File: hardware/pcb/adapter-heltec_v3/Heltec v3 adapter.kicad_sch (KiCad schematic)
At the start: 2 parts, among them U1 ESP32_LORA_V2.0

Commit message: Initial boards for raw prototyping
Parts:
- added C1: C_Polarized, Capacitor_THT:CP_Radial_D8.0mm_P3.50mm, symbol Device:C_Polarized
- added C2: C, Capacitor_THT:C_Rect_L4.0mm_W2.5mm_P2.50mm, symbol Device:C
- added J1: Conn_01x02_Pin, Connector_PinHeader_2.54mm:PinHeader_1x02_P2.54mm_Vertical, symbol Connector:Conn_01x02_Pin
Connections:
- net GND: now also U2.1 (GND_A), U2.16 (GND_D), U2.6 (GND_B), C1.2, C2.2, J1.2 (Pin_2)
- net VDD: now also U2.2 (VBAT_A), C1.1, C2.1, J1.1 (Pin_1); no longer U1.J2_3 (VEXT), U1.J2_4 (VEXT), U2.12 (VBAT_C)
- new net VEXT: U1.J2_3 (VEXT), U1.J2_4 (VEXT)

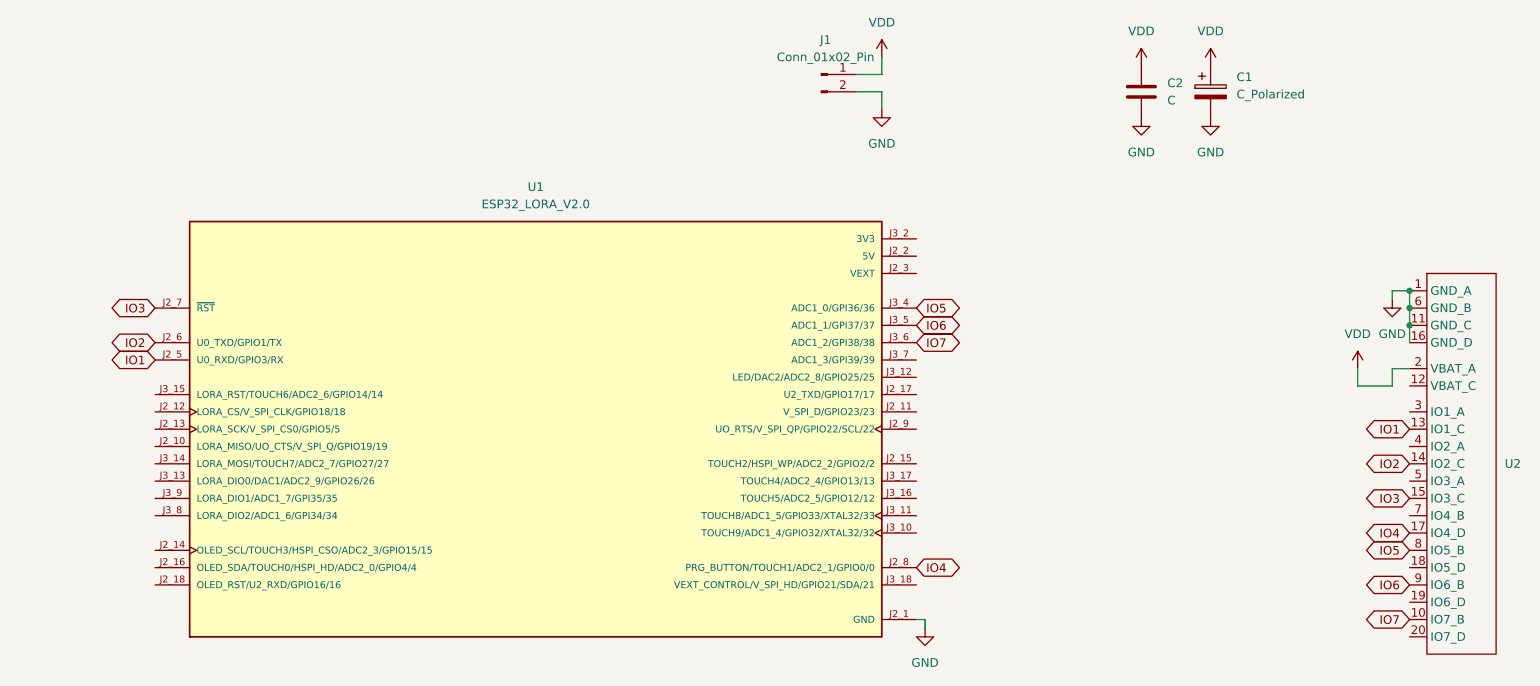
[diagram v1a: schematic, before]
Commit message: Update Heltec v3 adapter.kicad_sch
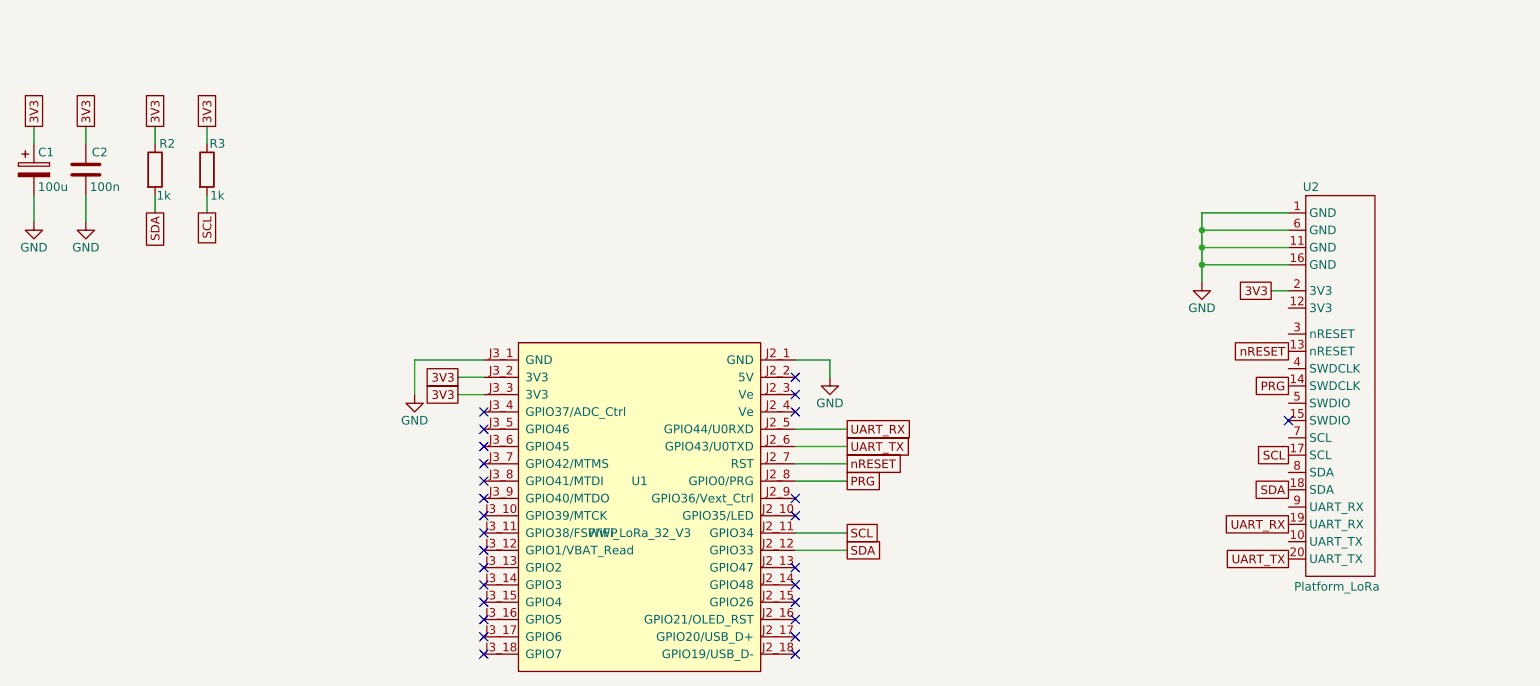
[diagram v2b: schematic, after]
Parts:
- removed J1: Conn_01x02_Pin, Connector_PinHeader_2.54mm:PinHeader_1x02_P2.54mm_Vertical, symbol Connector:Conn_01x02_Pin
- removed U1: ESP32_LORA_V2.0, Library:MODULE_ESP32_LORA_V2.0, symbol ESP32_LORA_V2.0:ESP32_LORA_V2.0
- removed U2: (no value), TwinOak platform footprints:platform-adapter-footprint, symbol TwinOak-standard-repeater-layout:Platform_interface
- added R2, R3: 1k, Resistor_SMD:R_0805_2012Metric_Pad1.20x1.40mm_HandSolder, symbol Device:R
- added U1: WiFi_LoRa_32_V3, Library:MODULE_ESP32_LORA_V2.0, symbol Heltec_V3:WiFi_LoRa_32_V3
- added U2: Platform_LoRa, TwinOak platform footprints:platform-adapter-footprint, symbol TwinOak-standard-repeater-layout:Platform_LoRa
- C1: value C_Polarized -> 100u
- C2: value C -> 100n
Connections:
- net VDD is gone; now on net 3V3: C1.1, C2.1
- net 3V3: now also R2.1, R3.1, U1.J3_2 (3V3), U1.J3_3 (3V3), U2.2 (3V3)
- net GND: now also U1.J2_1 (GND), U1.J3_1 (GND), U2.1 (GND), U2.11 (GND), U2.16 (GND), U2.6 (GND)
- new net PRG: U1.J2_8 (GPIO0/PRG), U2.14 (SWDCLK)
- new net SCL: R3.2, U1.J2_11 (GPIO34), U2.17 (SCL)
- new net SDA: R2.2, U1.J2_12 (GPIO33), U2.18 (SDA)
- new net UART_RX: U1.J2_5 (GPIO44/U0RXD), U2.19 (UART_RX)
- new net UART_TX: U1.J2_6 (GPIO43/U0TXD), U2.20 (UART_TX)
- new net nRESET: U1.J2_7 (RST), U2.13 (nRESET)
- no-connect marks 0 -> 27

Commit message: Cleanup
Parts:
- C1: value 100u -> 100u 16V; MPN (none) -> AISHI EWH1CM101E11OT
- C2: value 100n -> 10n; MPN (none) -> SR Passives CCT-10N/100V-S
- U1: footprint Library:MODULE_ESP32_LORA_V2.0 -> TwinOak:MODULE_ESP32_LORA_V2.0; symbol Heltec_V3:WiFi_LoRa_32_V3 -> TwinOak:WiFi_LoRa_32_V3
- U2: footprint TwinOak platform footprints:platform-adapter-footprint -> TwinOak:platform-adapter-footprint; symbol TwinOak-standard-repeater-layout:Platform_LoRa -> TwinOak:Platform_LoRa
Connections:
- net 3V3 renamed +3V3
- no-connect marks 27 -> 35
